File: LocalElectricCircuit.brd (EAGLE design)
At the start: 160 x 100 mm, 26 parts, among them IC1 PIC32MX360F512L, J1 Prog. Port, U1 ADS1118, U2 ADS1118

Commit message: Connected PIC32 analog pins
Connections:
- new net EXT_TEMP: IC1.41, X2.7
- new net RB_TEMP: IC1.42, X2.8
- net I_1_H: now also IC1.20
- net I_1_L: now also IC1.21
- net I_2_H: now also IC1.33
- net I_2_L: now also IC1.32
- net I_3_H: now also IC1.35
- net I_3_L: now also IC1.34
- net TEMP_1: now also IC1.25
- net TEMP_2: now also IC1.24
- net TEMP_3: now also IC1.22
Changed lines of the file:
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@@
 <signal name="TEMP_3">
 <contactref element="J2" pad="A3"/>
+<contactref element="IC1" pad="22"/>
+<wire x1="6.14" y1="-82.9" x2="154.666" y2="34.29" width="0" layer="19" extent="1-1"/>
 </signal>
 <signal name="GND_TEMP">
@@
 <signal name="TEMP_2">
 <contactref element="J2" pad="A4"/>
+<contactref element="IC1" pad="24"/>
+<wire x1="6.94" y1="-82.9" x2="154.666" y2="31.75" width="0" layer="19" extent="1-1"/>
 </signal>
 <signal name="TEMP_1">
 <contactref element="J2" pad="B4"/>
+<contactref element="IC1" pad="25"/>
+<wire x1="7.34" y1="-82.9" x2="152.126" y2="31.75" width="0" layer="19" extent="1-1"/>
 </signal>
 <signal name="GND_I_1">
@@
 <signal name="I_1_L">
 <contactref element="J2" pad="B5"/>
+<contactref element="IC1" pad="21"/>
+<wire x1="5.74" y1="-82.9" x2="152.126" y2="29.21" width="0" layer="19" extent="1-1"/>
 </signal>
 <signal name="I_1_H">
 <contactref element="J2" pad="C5"/>
+<contactref element="IC1" pad="20"/>
+<wire x1="5.34" y1="-82.9" x2="149.586" y2="29.21" width="0" layer="19" extent="1-1"/>
 </signal>
 <signal name="GND_I_2">
@@
 <signal name="I_2_L">
 <contactref element="J2" pad="B6"/>
+<contactref element="IC1" pad="32"/>
+<wire x1="9.24" y1="-78.6" x2="152.126" y2="26.67" width="0" layer="19" extent="1-1"/>
 </signal>
 <signal name="I_2_H">
 <contactref element="J2" pad="C6"/>
+<contactref element="IC1" pad="33"/>
+<wire x1="9.24" y1="-78.2" x2="149.586" y2="26.67" width="0" layer="19" extent="1-1"/>
 </signal>
 <signal name="GND_I_3">
@@
 <signal name="I_3_L">
 <contactref element="J2" pad="B7"/>
+<contactref element="IC1" pad="34"/>
+<wire x1="9.24" y1="-77.8" x2="152.126" y2="24.13" width="0" layer="19" extent="1-1"/>
 </signal>
 <signal name="I_3_H">
 <contactref element="J2" pad="C7"/>
+<contactref element="IC1" pad="35"/>
+<wire x1="9.24" y1="-77.4" x2="149.586" y2="24.13" width="0" layer="19" extent="1-1"/>
 </signal>
 <signal name="VERT_UP">
@@
 <contactref element="X1" pad="12"/>
 </signal>
+<signal name="EXT_TEMP">
+<contactref element="IC1" pad="41"/>
+<contactref element="X2" pad="7"/>
+<wire x1="11.429765625" y1="-3.43986875" x2="9.24" y2="-75" width="0" layer="19" extent="1-1"/>
+</signal>
+<signal name="RB_TEMP">
+<contactref element="IC1" pad="42"/>
+<contactref element="X2" pad="8"/>
+<wire x1="11.429765625" y1="-1.15386875" x2="9.24" y2="-74.6" width="0" layer="19" extent="1-1"/>
+</signal>
 </signals>

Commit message: Ballast pins added
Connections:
- new net BALLA1: IC1.77, X1.3
- new net BALLA2: IC1.78, X1.4
- new net BALLA3: IC1.81, X1.5
- new net BALLA4: IC1.82, X1.6
- new net BALLC1: IC1.83, X1.7
- new net BALLC2: IC1.84, X1.8
- new net BALLS1: IC1.72, X1.1
- new net BALLS2: IC1.76, X1.2
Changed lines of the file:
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@@
 <wire x1="11.429765625" y1="-1.15386875" x2="9.24" y2="-74.6" width="0" layer="19" extent="1-1"/>
+</signal>
+<signal name="BALLS2">
+<contactref element="IC1" pad="76"/>
+<contactref element="X1" pad="2"/>
+<wire x1="13.97" y1="29.199" x2="-4.16" y2="-71.4" width="0" layer="19" extent="1-1"/>
+</signal>
+<signal name="BALLA1">
+<contactref element="IC1" pad="77"/>
+<contactref element="X1" pad="3"/>
+<wire x1="13.97" y1="31.485" x2="-4.16" y2="-71.8" width="0" layer="19" extent="1-1"/>
+</signal>
+<signal name="BALLA2">
+<contactref element="IC1" pad="78"/>
+<contactref element="X1" pad="4"/>
+<wire x1="13.97" y1="33.771" x2="-4.16" y2="-72.2" width="0" layer="19" extent="1-1"/>
+</signal>
+<signal name="BALLA3">
+<contactref element="IC1" pad="81"/>
+<contactref element="X1" pad="5"/>
+<wire x1="13.97" y1="36.057" x2="-4.16" y2="-73.4" width="0" layer="19" extent="1-1"/>
+</signal>
+<signal name="BALLA4">
+<contactref element="IC1" pad="82"/>
+<contactref element="X1" pad="6"/>
+<wire x1="11.43" y1="25.77" x2="-4.16" y2="-73.8" width="0" layer="19" extent="1-1"/>
+</signal>
+<signal name="BALLC1">
+<contactref element="IC1" pad="83"/>
+<contactref element="X1" pad="7"/>
+<wire x1="11.43" y1="28.056" x2="-4.16" y2="-74.2" width="0" layer="19" extent="1-1"/>
+</signal>
+<signal name="BALLC2">
+<contactref element="IC1" pad="84"/>
+<contactref element="X1" pad="8"/>
+<wire x1="11.43" y1="30.342" x2="-4.16" y2="-74.6" width="0" layer="19" extent="1-1"/>
+</signal>
+<signal name="BALLS1">
+<contactref element="IC1" pad="72"/>
+<contactref element="X1" pad="1"/>
+<wire x1="13.97" y1="26.913" x2="-1.06" y2="-69.5" width="0" layer="19" extent="1-1"/>
 </signal>
 </signals>

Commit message: Added conductivity pins
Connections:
- new net COND_ENABLE_PIC: IC1.8
- net CHARGE_PROBE_0: now also IC1.6
- net CHARGE_PROBE_1: now also IC1.7
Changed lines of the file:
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@@
 <signal name="CHARGE_PROBE_0">
 <contactref element="J2" pad="A14"/>
+<contactref element="IC1" pad="6"/>
+<wire x1="-0.26" y1="-82.9" x2="154.666" y2="6.35" width="0" layer="19" extent="1-1"/>
 </signal>
 <signal name="CHARGE_PROBE_1">
 <contactref element="J2" pad="B14"/>
+<contactref element="IC1" pad="7"/>
+<wire x1="0.14" y1="-82.9" x2="152.126" y2="6.35" width="0" layer="19" extent="1-1"/>
 </signal>
 <signal name="COND_ENABLE">
@@
 <wire x1="13.97" y1="26.913" x2="-1.06" y2="-69.5" width="0" layer="19" extent="1-1"/>
 </signal>
+<signal name="COND_ENABLE_PIC">
+<contactref element="IC1" pad="8"/>
+</signal>
 </signals>

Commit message: aware of dog pleas pet dog
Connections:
- new net N$1: IC1.57, X2.4
- new net N$4: X2.5
- net RB_TEMP: now also IC1.56
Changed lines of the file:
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@@
 <?xml version="1.0" encoding="utf-8"?>
 <!DOCTYPE eagle SYSTEM "eagle.dtd">
-<eagle version="8.7.1">
+<eagle version="7.6.0">
 <drawing>
 <settings>
 <setting alwaysvectorfont="no"/>
-<setting keepoldvectorfont="yes"/>
 <setting verticaltext="up"/>
 </settings>
@@
 <param name="dpMaxLengthDifference" value="10mm"/>
 <param name="dpGapFactor" value="2.5"/>
+<param name="checkGrid" value="0"/>
 <param name="checkAngle" value="0"/>
 <param name="checkFont" value="1"/>
 <param name="checkRestrict" value="1"/>
-<param name="checkStop" value="0"/>
-<param name="checkValues" value="0"/>
 <param name="useDiameter" value="13"/>
 <param name="maxErrors" value="50"/>
@@
 <element name="C8" library="resistor" package="C1206" value="0.1uF" x="-59.69" y="-209.296"/>
 <element name="C9" library="resistor" package="C1206" value="0.1uF" x="-59.69" y="-215.392"/>
-<element name="PIC16" library="ic-package" library_urn="urn:adsk.eagle:library:239" package="DIL20" package3d_urn="urn:adsk.eagle:package:14436/1" value="pic16f689" x="-43.942" y="-228.854"/>
-<element name="PIC16_ICSP" library="pinhead" library_urn="urn:adsk.eagle:library:325" package="1X06" package3d_urn="urn:adsk.eagle:package:22472/2" value="" x="-48.006" y="-246.888"/>
+<element name="PIC16" library="ic-package" package="DIL20" value="pic16f689" x="-43.942" y="-228.854"/>
+<element name="PIC16_ICSP" library="pinhead" package="1X06" value="" x="-48.006" y="-246.888"/>
 <element name="C10" library="resistor" package="C1206" value="0.1uF" x="-59.69" y="-257.81"/>
 <element name="C11" library="resistor" package="C1206" value="0.01uF" x="-59.69" y="-264.16"/>
@@
 <contactref element="IC1" pad="42"/>
 <contactref element="X2" pad="8"/>
-<wire x1="11.429765625" y1="-1.15386875" x2="9.24" y2="-74.6" width="0" layer="19" extent="1-1"/>
+<contactref element="IC1" pad="56"/>
+<wire x1="5.34" y1="-69.5" x2="9.24" y2="-74.6" width="0" layer="19" extent="1-1"/>
+<wire x1="11.429765625" y1="-1.15386875" x2="5.34" y2="-69.5" width="0" layer="19" extent="1-1"/>
 </signal>
 <signal name="BALLS2">
@@
 <contactref element="IC1" pad="8"/>
 </signal>
+<signal name="N$1">
+<contactref element="X2" pad="4"/>
+<contactref element="IC1" pad="57"/>
+<wire x1="13.969765625" y1="2.27513125" x2="4.94" y2="-69.5" width="0" layer="19" extent="1-1"/>
+</signal>
+<signal name="N$4">
+<contactref element="X2" pad="5"/>
+</signal>
 </signals>
 </board>
 </drawing>
-<compatibility>
-<note version="8.2" severity="warning">
-Since Version 8.2, EAGLE supports online libraries. The ids
-of those online libraries will not be understood (or retained)
-with this version.
-</note>
-<note version="8.3" severity="warning">
-Since Version 8.3, EAGLE supports URNs for individual library
-assets (packages, symbols, and devices). The URNs of those assets
-will not be understood (or retained) with this version.
-</note>
-<note version="8.3" severity="warning">
-Since Version 8.3, EAGLE supports the association of 3D packages
-with devices in libraries, schematics, and board files. Those 3D
-packages will not be understood (or retained) with this version.
-</note>
-</compatibility>
 </eagle>

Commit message: Oh boy o"bertor
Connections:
- net N$1 renamed I2C_SCL
- removed net N$4: X2.5
- new net I2C_SDA: IC1.56, X2.5
- net RB_TEMP: no longer IC1.56
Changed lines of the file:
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@@
 <contactref element="IC1" pad="42"/>
 <contactref element="X2" pad="8"/>
-<contactref element="IC1" pad="56"/>
-<wire x1="5.34" y1="-69.5" x2="9.24" y2="-74.6" width="0" layer="19" extent="1-1"/>
-<wire x1="11.429765625" y1="-1.15386875" x2="5.34" y2="-69.5" width="0" layer="19" extent="1-1"/>
+<wire x1="11.429765625" y1="-1.15386875" x2="9.24" y2="-74.6" width="0" layer="19" extent="1-1"/>
 </signal>
 <signal name="BALLS2">
@@
 <contactref element="IC1" pad="8"/>
 </signal>
-<signal name="N$1">
+<signal name="I2C_SCL">
 <contactref element="X2" pad="4"/>
 <contactref element="IC1" pad="57"/>
 <wire x1="13.969765625" y1="2.27513125" x2="4.94" y2="-69.5" width="0" layer="19" extent="1-1"/>
 </signal>
-<signal name="N$4">
+<signal name="I2C_SDA">
 <contactref element="X2" pad="5"/>
+<contactref element="IC1" pad="56"/>
+<wire x1="13.969765625" y1="4.56113125" x2="5.34" y2="-69.5" width="0" layer="19" extent="1-1"/>
 </signal>
 </signals>

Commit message: Getting there
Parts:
- removed PIC16_ICSP: (no value), pinhead:1X06
- added C12, C13, C14, C15, C16, C17: 0.01uF, resistor:C1206
- added J3: Prog. Port, con-amp:520258-3
- added R5, R6, R8: 1k, rcl:0309/12
- added R7: 50k, rcl:M1206
- added T1: PN100, transistor:TO92
- R4: value 50k -> 1k; device rcl:M1206 -> rcl:0309/12
- moved PIC16 279.0 mm to (33.0, 39.4)
- moved R4 276.9 mm to (23.4, -6.60)
- moved R3 200.6 mm to (38.9, -28.4)
- moved C4 186.0 mm to (132.8, -193.0)
- moved R2 180.0 mm to (141.7, -172.5)
- moved C6 179.5 mm to (135.9, -182.1)
- moved SV1 171.5 mm to (130.3, -168.3)
- moved R1 167.4 mm to (130.3, -164.8)
- moved C2 158.0 mm to (116.5, -196.1)
- moved IC1 152.5 mm to (116.3, -177.8)
- moved U2 150.4 mm to (104.4, 28.7)
- moved U1 149.2 mm to (95.8, 28.4)
- moved C5 136.9 mm to (103.1, -184.4)
- moved C1 130.0 mm to (101.1, -175.1)
- moved C3 124.4 mm to (110.0, -164.2)
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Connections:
- removed net COND_ENABLE: J2.C14
- removed net COND_ENABLE_PIC: IC1.8
- new net CONDUCTIVITY_ENABLE_3V: IC1.8, R5.2
- new net CONDUCTIVITY_ENABLE_5V: J2.C14, R6.1, T1.2
- new net N$1: R5.1, T1.1
- net +3V3: now also C12.1, C13.1, C14.1, C15.1, C16.1, X1.13, X2.15, X2.8, X2.9
- net +3V3_PIC_ANALOG: now also C17.1
- net +5V: now also R6.2
- net EXT_TEMP: now also R8.1, X2.2; no longer X2.7
- net GND_3V3: now also C12.2, C13.2, C14.2, C15.2, C16.2, C17.2, J3.3, R4.2, R8.2, X1.10, X1.9, X2.12, X2.6; no longer PIC16_ICSP.3
- net GND_5V: now also T1.3
- net I2C_SCL: now also X2.13; no longer X2.4
- net I2C_SDA: now also X2.14; no longer X2.5
- net PIC16_3V3: now also J3.2, R7.1; no longer PIC16_ICSP.2, R4.2
- net PIC16_MCLR: now also J3.1, R7.2; no longer PIC16_ICSP.1, R4.1
- net PIC16_PGC: now also J3.5; no longer PIC16_ICSP.5
- net PIC16_PGD: now also J3.4; no longer PIC16_ICSP.4
- net RB_TEMP: now also R4.1, X2.1; no longer X2.8
- net U1RX: now also X2.4
- net U1TX: now also X2.5

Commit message: Started early layout
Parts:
- moved C9 343.9 mm to (132.1, 19.3)
- moved T1 310.0 mm to (105.9, 6.35), turned to 270 degrees
- moved R6 307.6 mm to (110.2, 13.0)
- moved R5 296.4 mm to (105.9, -4.06), turned to 270 degrees
- moved C11 295.6 mm to (34.5, 16.0)
- moved C10 295.6 mm to (34.5, 22.4)
- moved C8 285.2 mm to (120.7, 11.7), turned to 270 degrees
- moved C7 241.4 mm to (87.0, 12.6), turned to 270 degrees
- moved C17 241.0 mm to (93.5, 39.8), turned to 180 degrees
- moved C4 236.9 mm to (81.8, 38.4)
- moved C14 225.8 mm to (87.9, 40.4)
- moved C12 224.6 mm to (81.8, 41.2)
- moved C2 223.6 mm to (97.5, 26.7), turned to 270 degrees
- moved C5 223.3 mm to (87.9, 38.4), turned to 0 degrees
- moved C13 223.0 mm to (99.6, 26.7), turned to 270 degrees
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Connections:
- removed net GND_PROBE_1: J2.B11
- removed net GND_PROBE_2: J2.B12
- removed net GND_PROBE_DIFF: J2.B13
- removed net HOR_DIFF: U2.4
- removed net HOR_LEFT: U2.6
- removed net HOR_RIGHT: U1.6
- removed net VERT_DIFF: U1.5
- removed net VERT_DOWN: U2.5
- removed net VERT_UP: U1.4
- net GND_PROBE: now also J2.B11, J2.B12, J2.B13
- net PROBE_DIFF_HOR: now also U2.4
- net PROBE_DIFF_VERT: now also U1.5
- net PROBE_HOR_1_RIGHT: now also U1.6
- net PROBE_HOR_2_LEFT: now also U2.6
- net PROBE_VERT_1_UP: now also U1.4
- net PROBE_VERT_2_DOWN: now also U2.5
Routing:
- net +3V3: track 0.00 -> 81.3 mm
- net GND_3V3: track 0.00 -> 78.2 mm, vias 0 -> 1
- net OSC2: track 0.00 -> 22.2 mm
- net I_1_H: track 0.00 -> 18.0 mm
- net OSC1: track 0.00 -> 16.1 mm
- net +3V3_PIC_ANALOG: track 0.00 -> 13.7 mm
- net VCAP/VCORE: track 0.00 -> 4.93 mm

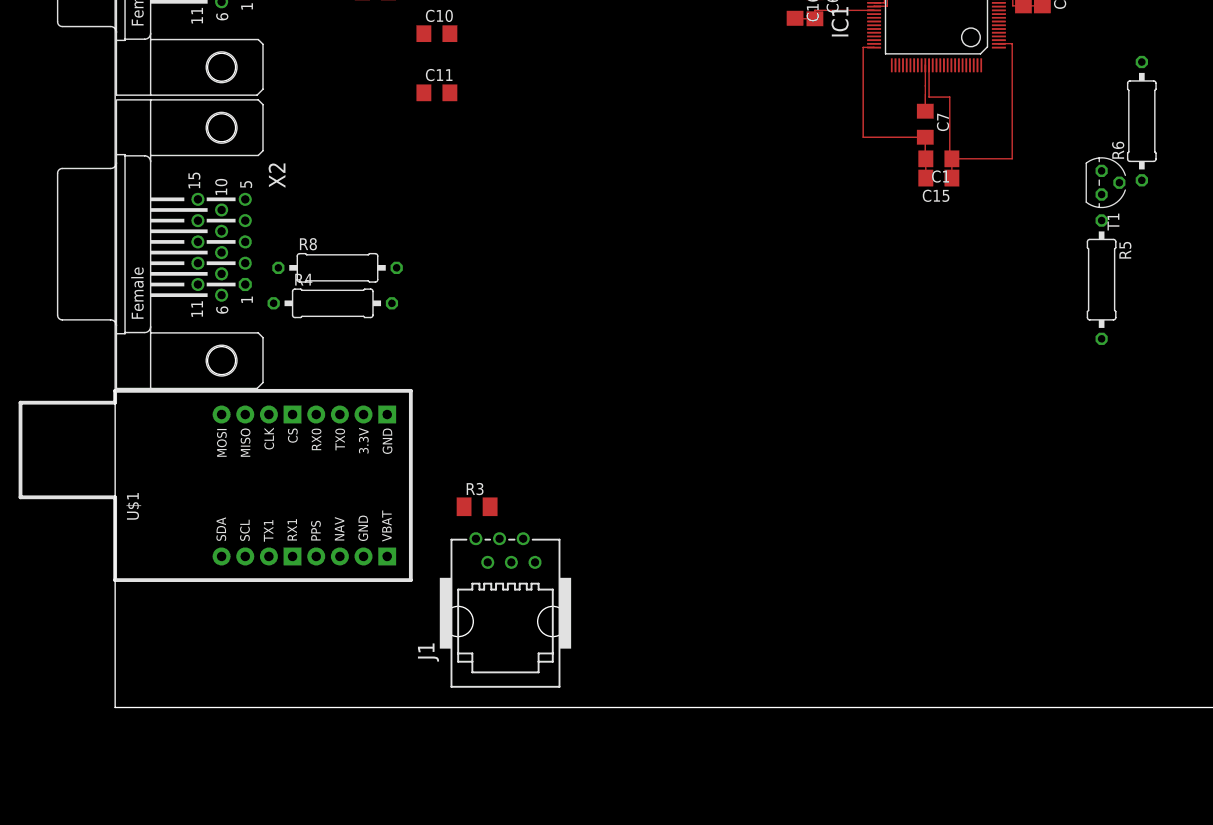
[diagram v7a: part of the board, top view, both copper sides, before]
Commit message: Transistor circuit updated to be active high and to save power.
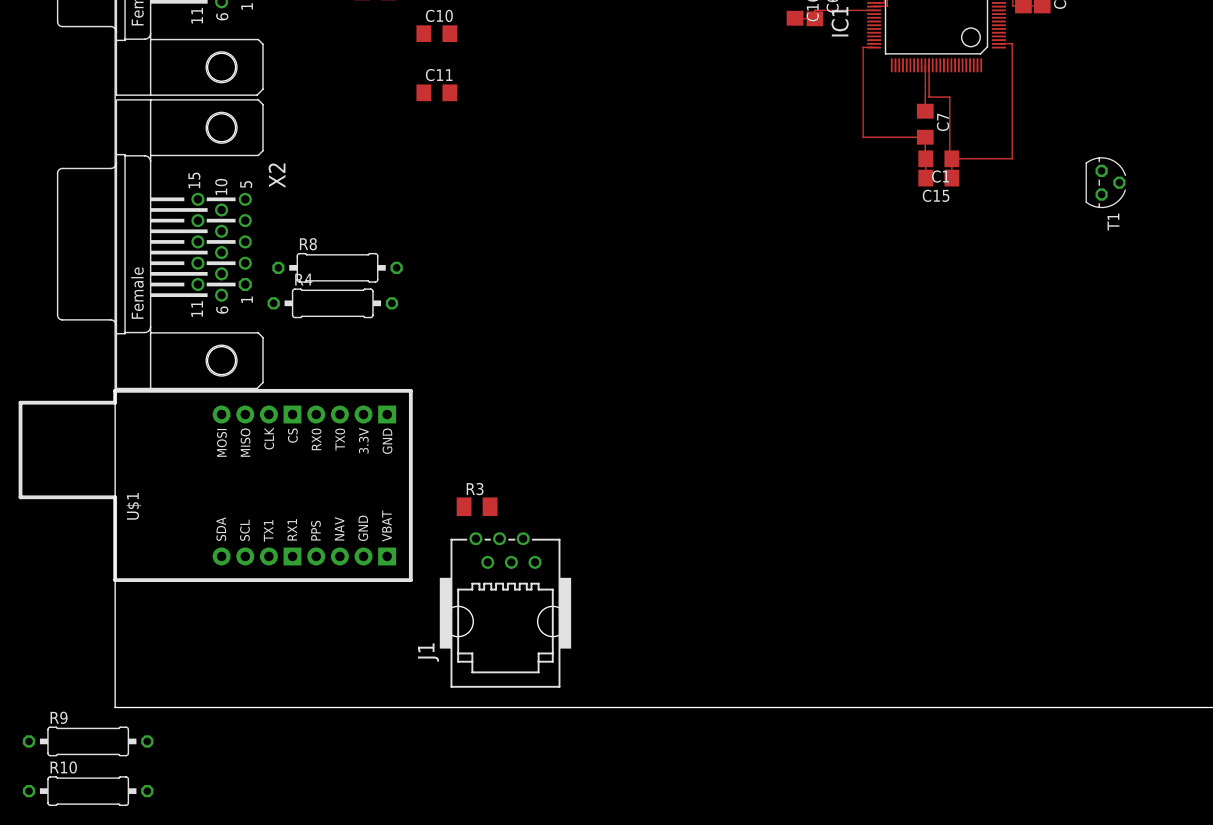
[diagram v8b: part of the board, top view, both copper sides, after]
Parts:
- removed R5, R6: 1k, rcl:0309/12
- added R10, R9: 1k, rcl:0309/12
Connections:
- removed net N$1: R5.1, T1.1
- new net N$5: R9.2, T1.3
- net +5V: now also T1.2; no longer R6.2
- net CONDUCTIVITY_ENABLE_3V: now also T1.1; no longer R5.2
- net CONDUCTIVITY_ENABLE_5V: now also R10.2, R9.1; no longer R6.1, T1.2
- net GND_5V: now also R10.1; no longer T1.3
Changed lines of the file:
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@@
 <element name="C10" library="resistor" package="C1206" value="0.1uF" x="34.544" y="22.352"/>
 <element name="C11" library="resistor" package="C1206" value="0.01uF" x="34.544" y="16.002"/>
-<element name="R5" library="rcl" package="0309/12" value="1k" x="105.918" y="-4.064" rot="R270"/>
 <element name="T1" library="transistor" package="TO92" value="PN100" x="105.918" y="6.35" rot="R270"/>
-<element name="R6" library="rcl" package="0309/12" value="1k" x="110.236" y="12.954" rot="R90"/>
 <element name="J3" library="con-amp" package="520258-3" value="Prog. Port" x="56.896" y="38.608" rot="R180"/>
 <element name="R7" library="rcl" package="M1206" value="50k" x="27.94" y="26.924"/>
@@
 <element name="R4" library="rcl" package="0309/12" value="1k" x="23.368" y="-6.604"/>
 <element name="R8" library="rcl" package="0309/12" value="1k" x="23.876" y="-2.794"/>
+<element name="R9" library="rcl" package="0309/12" value="1k" x="-2.8956" y="-53.6448"/>
+<element name="R10" library="rcl" package="0309/12" value="1k" x="-2.8956" y="-58.9788"/>
 </elements>
 <signals>
@@
 <contactref element="C9" pad="2"/>
 <contactref element="U1" pad="2"/>
-<contactref element="T1" pad="3"/>
+<contactref element="R10" pad="1"/>
 <wire x1="134.874" y1="17.254" x2="149.586" y2="34.29" width="0" layer="19" extent="1-1"/>
 <wire x1="134.374" y1="17.254" x2="134.874" y2="17.254" width="0" layer="19" extent="1-1"/>
@@
 <wire x1="122.944" y1="9.634" x2="123.444" y2="9.634" width="0" layer="19" extent="1-1"/>
 <wire x1="120.65" y1="10.284" x2="122.944" y2="9.634" width="0" layer="19" extent="1-1"/>
-<wire x1="105.918" y1="7.62" x2="120.65" y2="10.284" width="0" layer="19" extent="1-1"/>
+<wire x1="-9.2456" y1="-58.9788" x2="120.65" y2="10.284" width="0" layer="19" extent="1-1"/>
 </signal>
 <signal name="+5V">
@@
 <contactref element="C8" pad="1"/>
 <contactref element="C9" pad="1"/>
-<contactref element="R6" pad="2"/>
+<contactref element="T1" pad="2"/>
 <wire x1="134.874" y1="21.354" x2="149.586" y2="31.75" width="0" layer="19" extent="1-1"/>
 <wire x1="132.08" y1="20.704" x2="134.874" y2="21.354" width="0" layer="19" extent="1-1"/>
 <wire x1="123.444" y1="13.734" x2="132.08" y2="20.704" width="0" layer="19" extent="1-1"/>
 <wire x1="120.65" y1="13.084" x2="123.444" y2="13.734" width="0" layer="19" extent="1-1"/>
-<wire x1="110.236" y1="19.304" x2="120.65" y2="13.084" width="0" layer="19" extent="1-1"/>
+<wire x1="107.823" y1="6.35" x2="120.65" y2="13.084" width="0" layer="19" extent="1-1"/>
 </signal>
 <signal name="U2RX">
@@
 <wire x1="8.889765625" y1="2.27513125" x2="81.4888" y2="28.454" width="0" layer="19" extent="1-1"/>
 </signal>
-<signal name="N$1">
+<signal name="CONDUCTIVITY_ENABLE_5V">
+<contactref element="J2" pad="C14"/>
+<contactref element="R9" pad="1"/>
+<contactref element="R10" pad="2"/>
+<wire x1="3.4544" y1="-58.9788" x2="149.586" y2="6.35" width="0" layer="19" extent="1-1"/>
+<wire x1="-9.2456" y1="-53.6448" x2="3.4544" y2="-58.9788" width="0" layer="19" extent="1-1"/>
+</signal>
+<signal name="CONDUCTIVITY_ENABLE_3V">
+<contactref element="IC1" pad="8"/>
 <contactref element="T1" pad="1"/>
-<contactref element="R5" pad="1"/>
-<wire x1="105.918" y1="2.286" x2="105.918" y2="5.08" width="0" layer="19" extent="1-1"/>
-</signal>
-<signal name="CONDUCTIVITY_ENABLE_5V">
-<contactref element="T1" pad="2"/>
-<contactref element="R6" pad="1"/>
-<contactref element="J2" pad="C14"/>
-<wire x1="110.236" y1="6.604" x2="149.586" y2="6.35" width="0" layer="19" extent="1-1"/>
-<wire x1="107.823" y1="6.35" x2="110.236" y2="6.604" width="0" layer="19" extent="1-1"/>
-</signal>
-<signal name="CONDUCTIVITY_ENABLE_3V">
-<contactref element="R5" pad="2"/>
-<contactref element="IC1" pad="8"/>
-<wire x1="94.8888" y1="23.654" x2="105.918" y2="-10.414" width="0" layer="19" extent="1-1"/>
+<wire x1="105.918" y1="5.08" x2="94.8888" y2="23.654" width="0" layer="19" extent="1-1"/>
+</signal>
+<signal name="N$5">
+<contactref element="R9" pad="2"/>
+<contactref element="T1" pad="3"/>
+<wire x1="3.4544" y1="-53.6448" x2="105.918" y2="7.62" width="0" layer="19" extent="1-1"/>
 </signal>
 </signals>
